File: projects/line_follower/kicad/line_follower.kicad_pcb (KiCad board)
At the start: 2 copper layers, 48.3 x 48.3 mm, 37 parts, among them P1 I2C, P2 RST, P3 HC-SR04, P4 MOTOR_L, P5 MOTOR_R, P6 BATT, Q1 PHOTO_TRANSISTOR, Q2 PHOTO_TRANSISTOR, Q3 PHOTO_TRANSISTOR, Q4 PHOTO_TRANSISTOR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

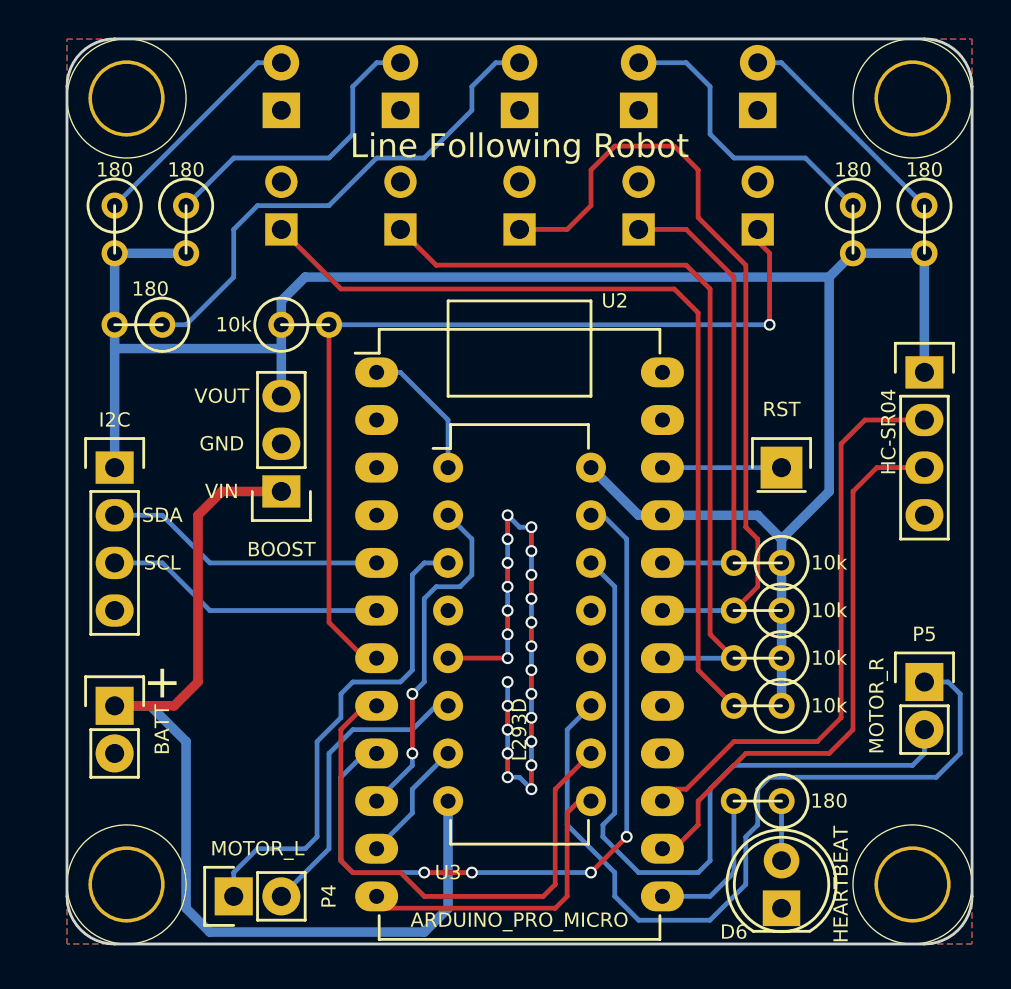
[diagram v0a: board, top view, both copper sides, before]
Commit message: Adding a button to line follower; rerouting most traces for cleaner design and better heat dissipation
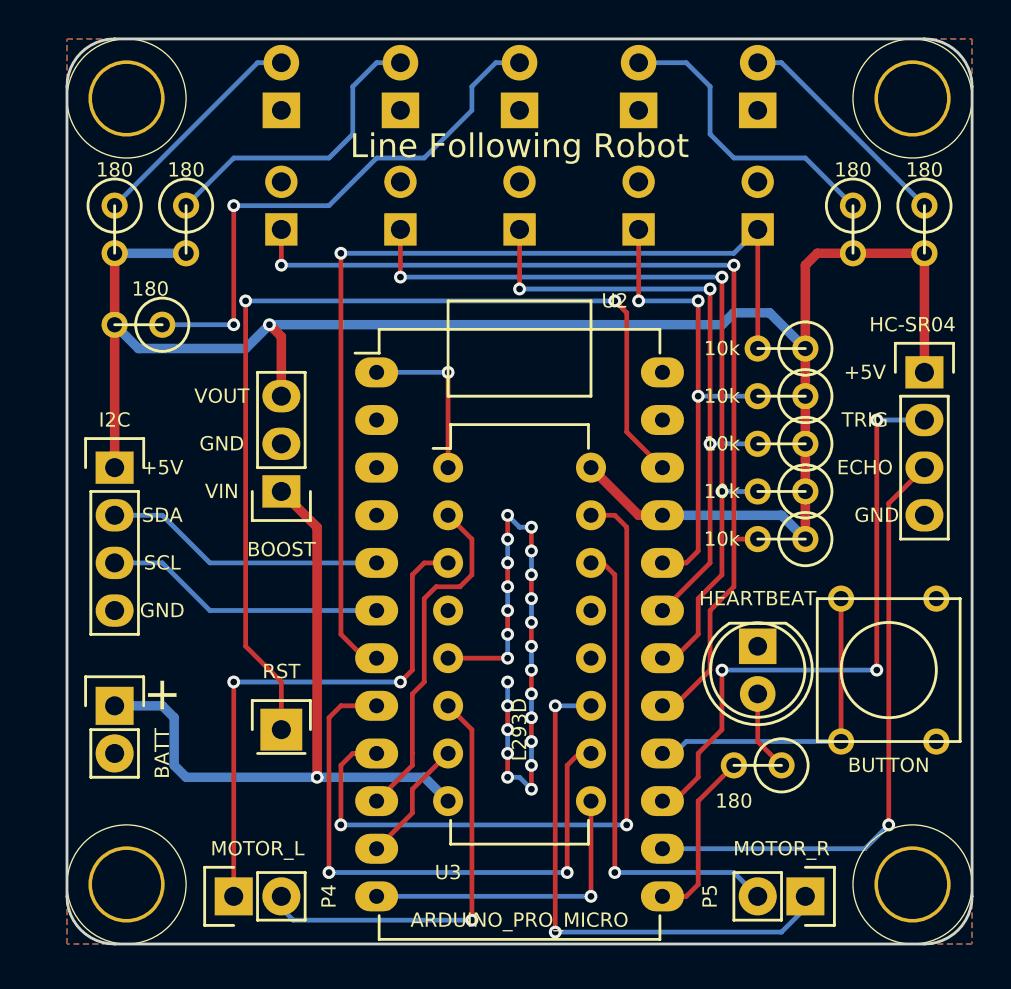
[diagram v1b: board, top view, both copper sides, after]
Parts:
- added SW1: BUTTON, Buttons_Switches_ThroughHole:SW_PUSH_SMALL, F.Cu at (87.0, 94.6)
- moved P2 30.1 mm to (54.6, 97.8)
- moved R6 25.4 mm to (81.3, 77.5), turned to 180 degrees
- moved D6 14.0 mm to (80.0, 93.3), turned to 270 degrees
- moved P5 13.1 mm to (82.5, 106.7), turned to 270 degrees
- moved R10 8.98 mm to (81.3, 80.0)
- moved R7 8.98 mm to (81.3, 87.6)
- moved R8 8.98 mm to (81.3, 85.1)
- moved R9 8.98 mm to (81.3, 82.5)
- moved MP6 4.49 mm to (49.5, 92.1)
- moved MP5 4.44 mm to (53.3, 92.1)
- moved R11 1.91 mm to (80.0, 99.7)
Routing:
- net Net-(P2-Pad1): track 6.35 -> 54.0 mm, vias 0 -> 2
- net Net-(SW1-Pad2): track 0.00 -> 17.4 mm
- net +BATT: track 53.1 -> 37.4 mm, vias 0 -> 1
- net Net-(P5-Pad1): track 42.9 -> 28.5 mm, vias 0 -> 2
- net Net-(P5-Pad2): track 39.5 -> 26.5 mm, vias 0 -> 1
- net /ADC_3: track 42.2 -> 34.1 mm, vias 0 -> 3
- net +5V: track 106.6 -> 98.8 mm, vias 0 -> 1
- net /ADC_1: track 46.3 -> 53.8 mm, vias 0 -> 2
- net Net-(P4-Pad2): track 16.1 -> 23.0 mm, vias 0 -> 1
- net /ADC_5: track 48.0 -> 51.9 mm
- net Net-(P4-Pad1): track 26.2 -> 29.4 mm, vias 0 -> 2
- net /DIST_TRIG: track 30.9 -> 33.7 mm, vias 0 -> 3
- net /ADC_2: track 41.8 -> 44.5 mm, vias 0 -> 3
- net /DIST_ECHO: track 30.6 -> 33.1 mm, vias 0 -> 1
- net Net-(D3-Pad2): track 27.1 -> 29.3 mm, vias 0 -> 2
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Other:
- net class Default: clearance 0.2 -> 0.1524; via_dia 0.635 -> 0.6858; via_drill 0.4064 -> 0.3556
- net class Power: clearance 0.2 -> 0.1524; via_dia 0.635 -> 0.6858; via_drill 0.4064 -> 0.3556
- rule trace_clearance: 0.2 -> 0.1524
- rule trace_min: 0.2 -> 0.2032
- rule via_min_drill: 0.3 -> 0.3048
- rule via_min_size: 0.4 -> 0.508

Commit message: Commit final version of the PCB; this is what we ordered
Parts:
- added C1: CAP, Capacitors_THT:C_Radial_D8_L13_P3.8, F.Cu at (45.7, 76.2)
- R1, R11, R2, R3, R4, R5: value 180 -> 220
- moved P2 32.5 mm to (87.0, 101.0)
- moved R7 12.7 mm to (81.3, 74.9)
- moved R3 5.99 mm to (50.2, 71.1), turned to 270 degrees
- moved P1 2.54 mm to (45.7, 86.4)
- moved P6 1.91 mm to (45.7, 98.4)
- moved R2 1.91 mm to (47.6, 71.1)
- moved R4 1.27 mm to (86.4, 71.1)
- moved R1 0.63 mm to (45.1, 71.1)
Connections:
- U2 pad 13: Net-(R11-Pad2) -> /DIST_ECHO
- U2 pad 14: /DIST_ECHO -> Net-(SW1-Pad2)
- U2 pad 15: /DIST_TRIG -> Net-(R11-Pad2)
- U2 pad 16: Net-(SW1-Pad2) -> /DIST_TRIG
- U2 pad 17: /ADC_1 -> /ADC_5
- U2 pad 7: /ADC_5 -> /ADC_1
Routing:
- net GND: track 32.9 -> 61.4 mm, vias 24 -> 39
- net Net-(P2-Pad1): track 54.0 -> 30.0 mm, vias 2 -> 1
- net /ADC_5: track 51.9 -> 29.1 mm, vias 1 -> 0
- net Net-(D3-Pad2): track 29.3 -> 21.0 mm, vias 2 -> 0
- net /ADC_2: track 44.5 -> 51.0 mm, vias 3 -> 1
- net /DIST_TRIG: track 33.7 -> 27.3 mm, vias 3 -> 0
- net /MOTOR_R_4A: track 40.5 -> 45.8 mm
- net Net-(SW1-Pad2): track 17.4 -> 22.5 mm
- net /MOTOR_R_3A: track 31.6 -> 36.6 mm
- net +BATT: track 37.4 -> 41.7 mm
- net /ADC_1: track 53.8 -> 50.3 mm, vias 2 -> 1
- net /DIST_ECHO: track 33.1 -> 36.4 mm, vias 1 -> 0
- net Net-(R11-Pad2): track 9.31 -> 5.98 mm
- net Net-(P4-Pad1): track 29.4 -> 27.4 mm, vias 2 -> 0
- net Net-(D2-Pad2): track 16.1 -> 18.0 mm
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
